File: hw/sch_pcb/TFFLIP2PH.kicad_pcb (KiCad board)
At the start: 2 copper layers, 65.3 x 15.7 mm, 2 parts, among them J1 Flipper_Zero

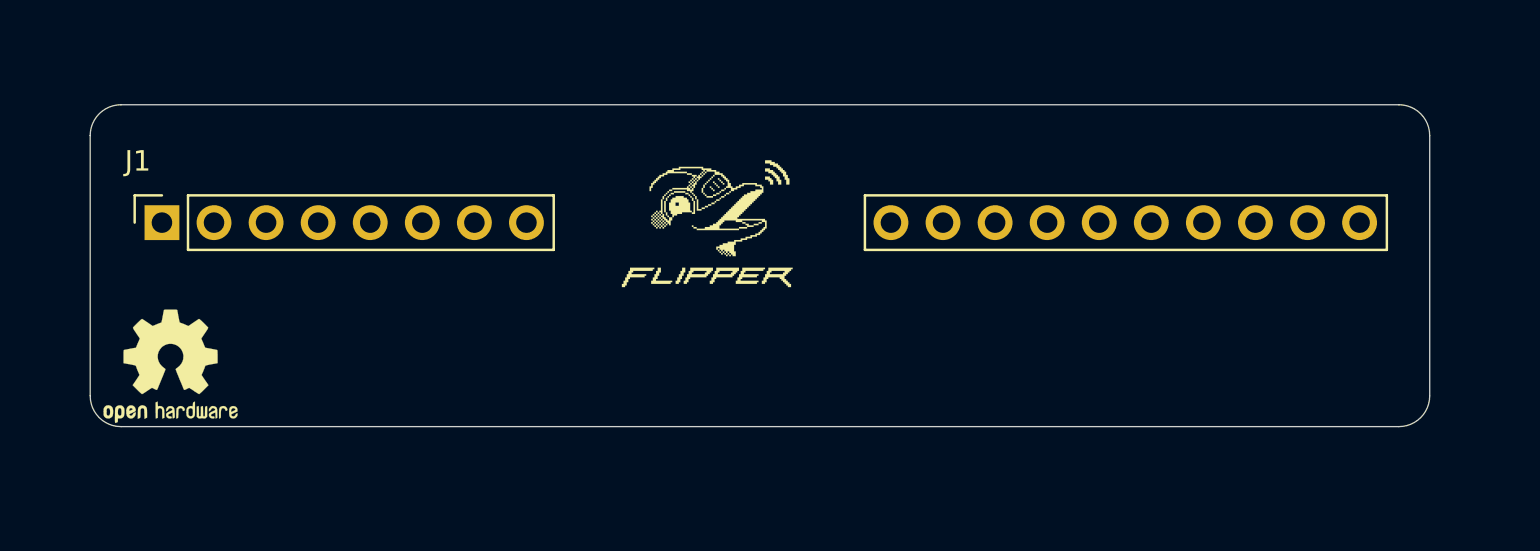
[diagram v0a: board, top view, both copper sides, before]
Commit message: Swap board sides to match top view on flipper zero.
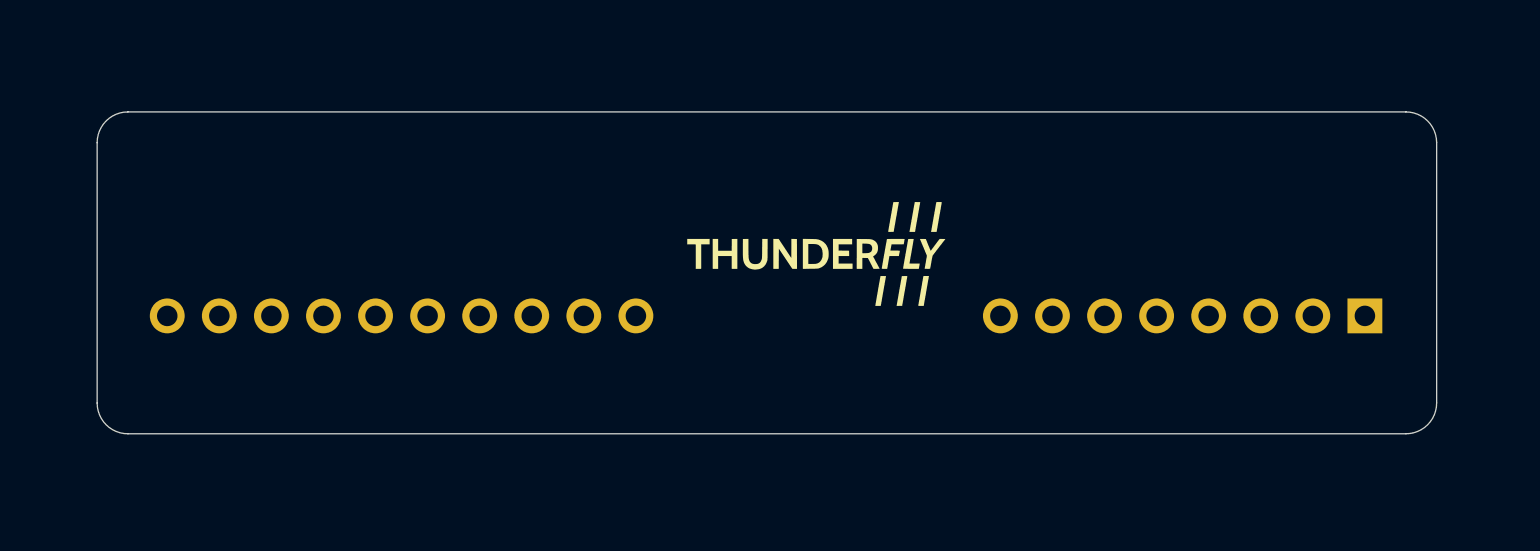
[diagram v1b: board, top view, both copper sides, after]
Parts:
- removed REF**: OSHW-Logo2_7.3x6mm_SilkScreen, Symbol:OSHW-Logo2_7.3x6mm_SilkScreen
- added G1: LOGO, TF_LOGA:TF 14x6,6, F.Cu at (144.4, 114.5)
- J1: moved to B.Cu
- moved J1 58.9 mm to (171.3, 117.5), turned to 180 degrees

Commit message: Fix pin-header orientation.
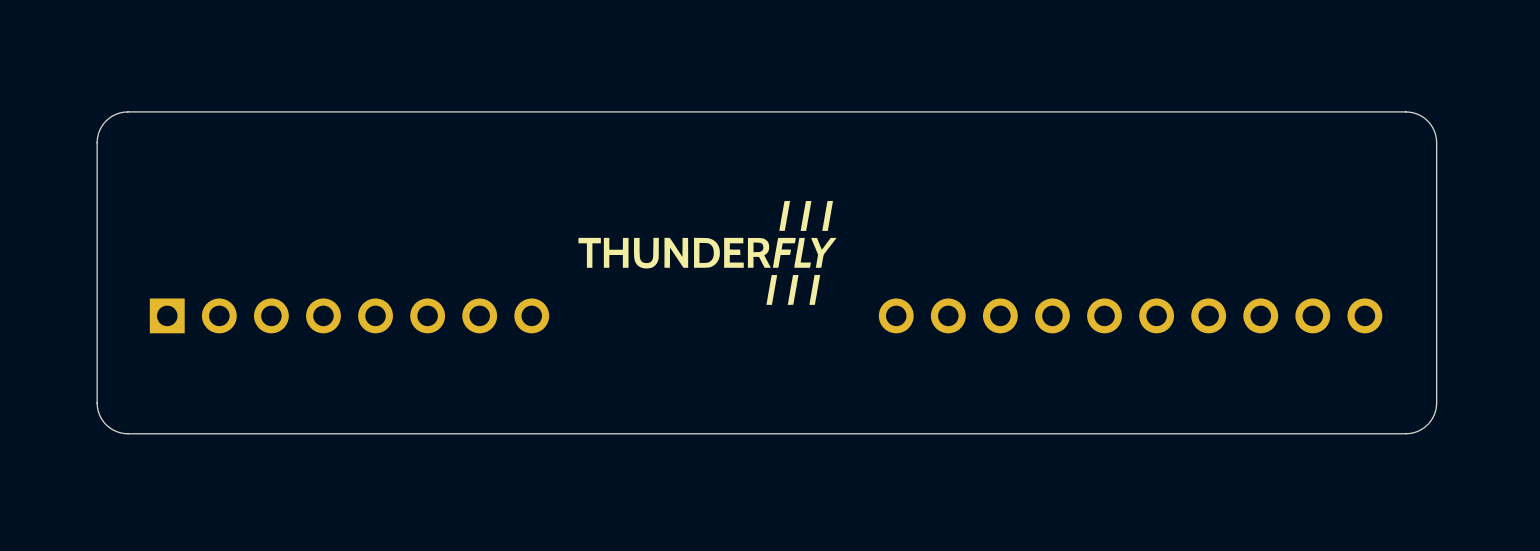
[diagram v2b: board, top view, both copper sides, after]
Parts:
- moved J1 58.4 mm to (112.8, 117.5), turned to 0 degrees
- moved G1 5.31 mm to (139.1, 114.5)

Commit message: Restore accidentally deleted OSHW logo.
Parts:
- added REF**: OSHW-Logo2_7.3x6mm_SilkScreen, Symbol:OSHW-Logo2_7.3x6mm_SilkScreen, B.Cu at (170.4, 111.5)

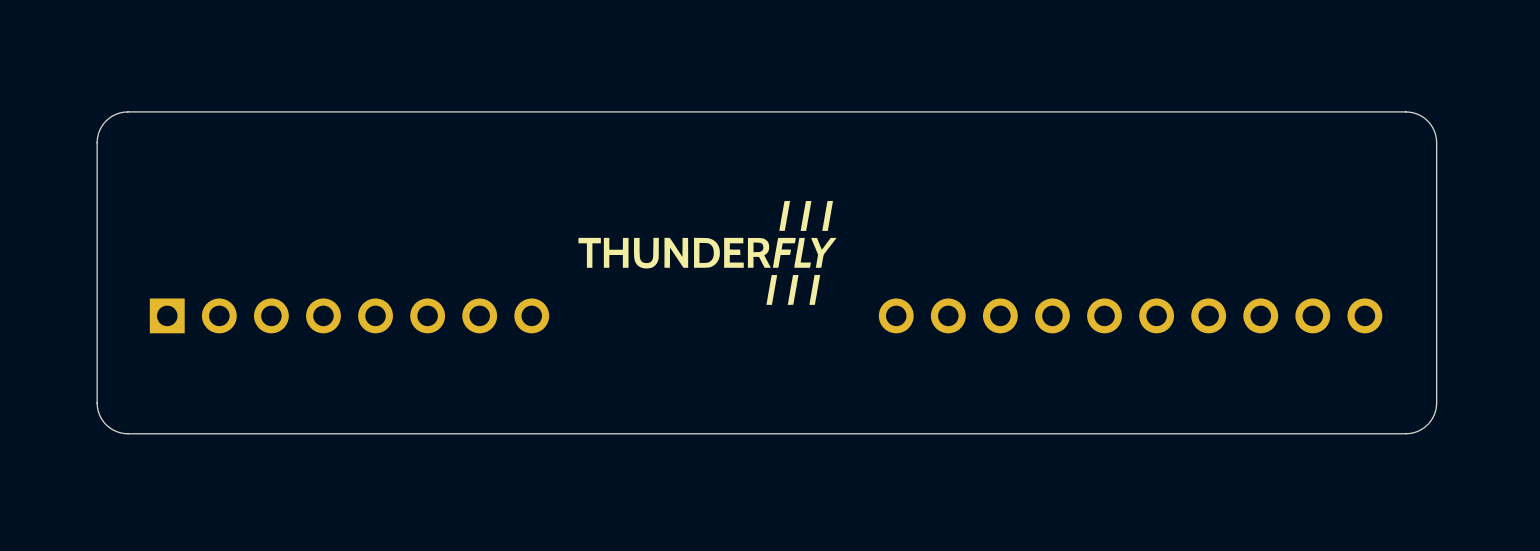
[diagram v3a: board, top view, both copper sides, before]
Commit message: Initial set of connectors.
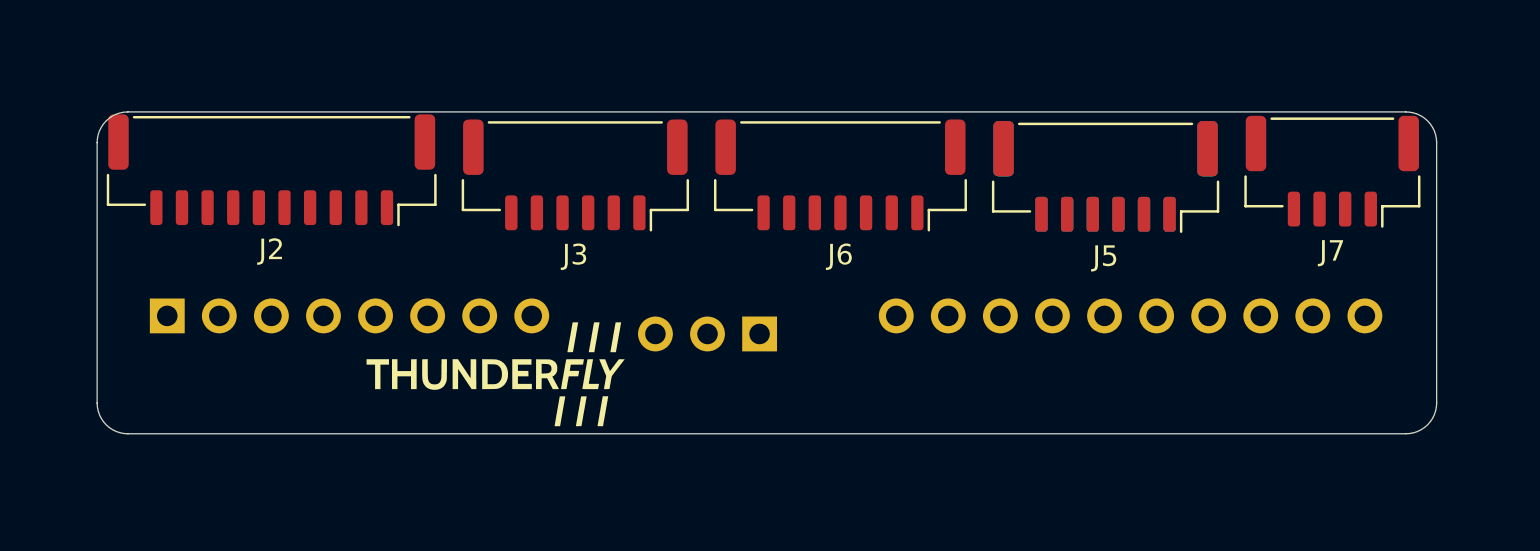
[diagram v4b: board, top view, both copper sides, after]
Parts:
- added J2: SM10B-GHS-TB, Connector_JST:JST_GH_SM10B-GHS-TB_1x10-1MP_P1.25mm_Horizontal, F.Cu at (117.9, 110.4)
- added J3: SM06B-GHS-TB, Connector_JST:JST_GH_SM06B-GHS-TB_1x06-1MP_P1.25mm_Horizontal, F.Cu at (132.7, 110.7)
- added J4: Angled Pinheader, Connector_PinHeader_2.54mm:PinHeader_1x03_P2.54mm_Horizontal, B.Cu at (141.7, 118.4)
- added J5: SM06B-GHS-TB, Connector_JST:JST_GH_SM06B-GHS-TB_1x06-1MP_P1.25mm_Horizontal, F.Cu at (158.6, 110.7)
- added J6: SM07B-GHS-TB, Connector_JST:JST_GH_SM07B-GHS-TB_1x07-1MP_P1.25mm_Horizontal, F.Cu at (145.7, 110.7)
- added J7: SM04B-GHS-TB, Connector_JST:JST_GH_SM04B-GHS-TB_1x04-1MP_P1.25mm_Horizontal, F.Cu at (169.7, 110.5)
- added J8: SM06B-GHS-TB, Connector_JST:JST_GH_SM06B-GHS-TB_1x06-1MP_P1.25mm_Horizontal, B.Cu at (158.6, 110.7)
- moved G1 11.9 mm to (128.8, 120.4)

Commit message: Routing in progress.
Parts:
- added J9: SM08B-GHS-TB, Connector_JST:JST_GH_SM08B-GHS-TB_1x08-1MP_P1.25mm_Horizontal, B.Cu at (155.0, 110.5)
- moved J8 31.6 mm to (127.0, 110.5)
- moved J2 0.37 mm to (118.3, 110.5)
- moved J3 0.33 mm to (133.0, 110.5)
- moved J5 0.27 mm to (158.7, 110.5)
- moved J6 0.26 mm to (145.9, 110.5)
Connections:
- J1 pad 10: unconnected-(J1-PA14-Pad10) -> /TIMEPULSE
- J1 pad 12: unconnected-(J1-PA13-Pad12) -> /EXTINT
- J1 pad 13: unconnected-(J1-PB6-Pad13) -> /TXD
- J1 pad 14: unconnected-(J1-PB7-Pad14) -> /RXD
- J1 pad 15: unconnected-(J1-PC1-Pad15) -> /SDA
- J1 pad 16: unconnected-(J1-PC0-Pad16) -> /SCL
- J1 pad 17: unconnected-(J1-PB14-Pad17) -> /BUZZER
- J1 pad 2: unconnected-(J1-PA7-Pad2) -> /MOSI
- J1 pad 3: unconnected-(J1-PA6-Pad3) -> /#CTS
- J1 pad 4: unconnected-(J1-PA4-Pad4) -> /SS1
- J1 pad 5: unconnected-(J1-PB3-Pad5) -> /#RTS
- J1 pad 6: unconnected-(J1-PB2-Pad6) -> /SS2
- J1 pad 7: unconnected-(J1-PC3-Pad7) -> /GEO_STAT
- J2 pad 1: +5VA -> +5V
- J2 pad 2: /RX -> /TXD
- J2 pad 3: /TX -> /RXD
- J2 pad 4: /SCL1 -> /SCL
- J2 pad 5: /SDA1 -> /SDA
- J2 pad 6: /SAFETY_SW -> /GEO_STAT
- J2 pad 7: /SAFETY_SW_LED -> /EXTINT
- J2 pad 8: /SAFE_VCC -> +3.3V
- J3 pad 2: /RX -> /TXD
- J3 pad 3: /TX -> /RXD
- J3 pad 4: /I2C2.SCL -> /SCL
- J3 pad 5: /I2C2.SDA -> /SDA
- J4 pad 1: /PWM -> /MOSI
- J6 pad 2: /SCK -> /#RTS
- J6 pad 3: /MISO -> /#CTS
- J6 pad 5: /#CS -> /SS1
- J6 pad 6: unconnected-(J6-Pad6) -> /SS2
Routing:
- net +5V: track 0.00 -> 107.3 mm
- net /SCL: track 0.00 -> 80.9 mm, vias 0 -> 2
- net /SDA: track 0.00 -> 73.7 mm, vias 0 -> 2
- net /RXD: track 0.00 -> 66.0 mm, vias 0 -> 7
- net /BUZZER: track 0.00 -> 64.1 mm
- net /#CTS: track 0.00 -> 54.5 mm, vias 0 -> 1
- net /#RTS: track 0.00 -> 51.2 mm, vias 0 -> 2
- net +3.3V: track 0.00 -> 49.9 mm, vias 0 -> 1
- net /GEO_STAT: track 0.00 -> 48.0 mm, vias 0 -> 2
- net /EXTINT: track 0.00 -> 46.5 mm, vias 0 -> 1
- net /MOSI: track 0.00 -> 37.1 mm
- net /SS1: track 0.00 -> 30.4 mm
- net /SS2: track 0.00 -> 22.1 mm
- net /TXD: track 0.00 -> 16.1 mm, vias 0 -> 2
- net GND: track 0.00 -> 14.4 mm, vias 0 -> 6
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- added copper zone on B.Cu, net GND
- added copper zone on F.Cu, net GND
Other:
- rule pad_to_mask_clearance: 0 -> 0.05

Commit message: Fully routed PCB.
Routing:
- net +5V: track 107.3 -> 165.7 mm
- net GND: track 14.4 -> 63.8 mm, vias 6 -> 10
- net /TXD: track 16.1 -> 53.4 mm, vias 2 -> 3
- net /RXD: track 66.0 -> 62.4 mm
- net /GEO_STAT: track 48.0 -> 45.3 mm
- net /#RTS: track 51.2 -> 49.0 mm
- net /MOSI: track 37.1 -> 38.1 mm
- net /SDA: track 73.7 -> 72.7 mm
- net /BUZZER: track 64.1 -> 63.3 mm
- net /EXTINT: track 46.5 -> 47.1 mm

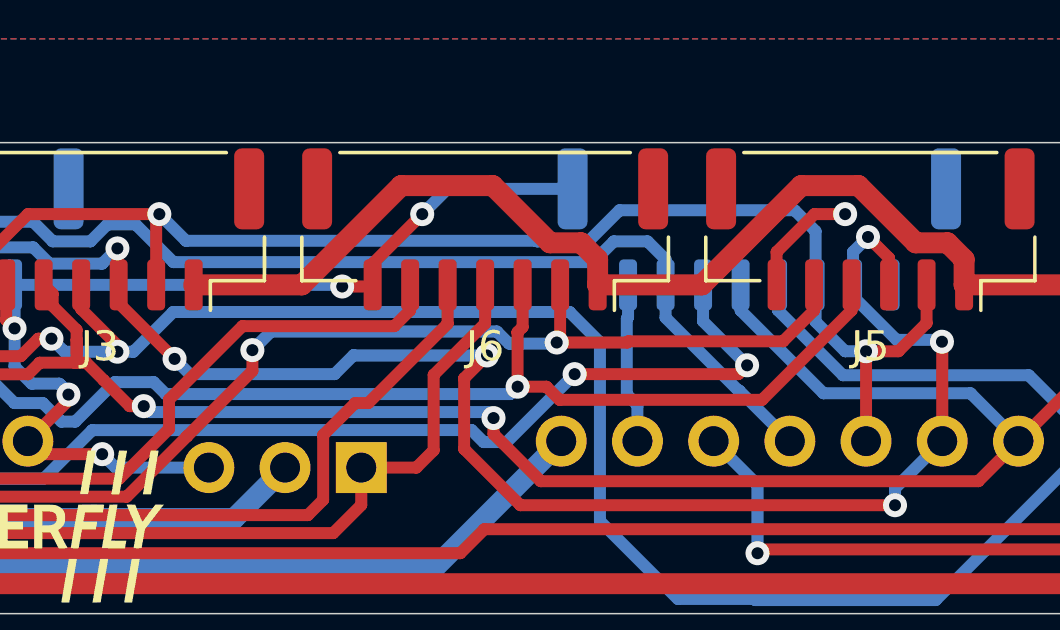
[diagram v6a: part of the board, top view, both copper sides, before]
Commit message: Fix DRC errors.
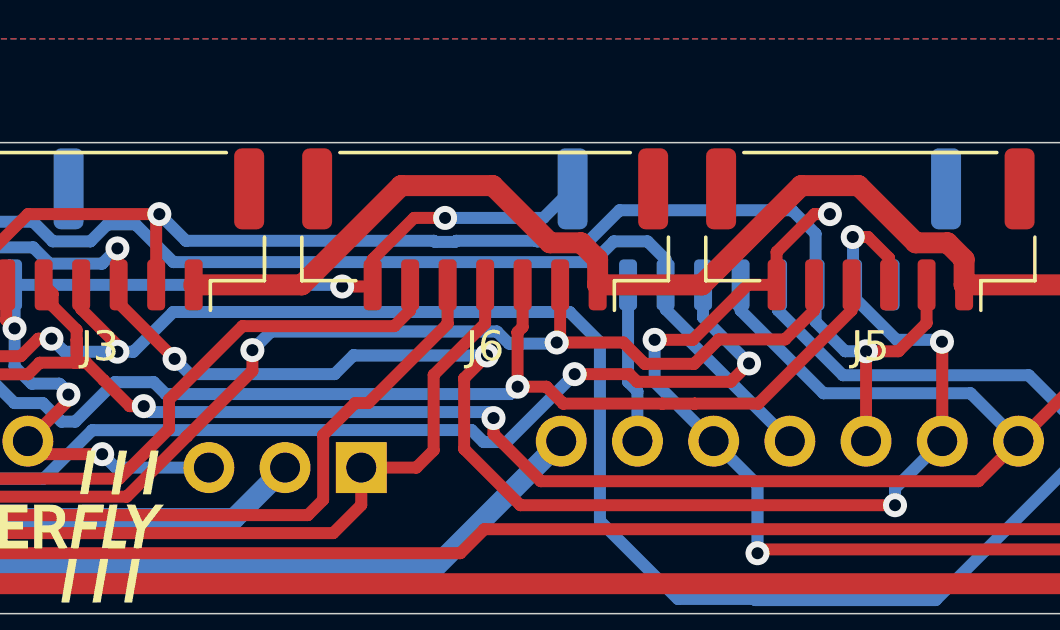
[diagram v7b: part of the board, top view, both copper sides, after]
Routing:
- net GND: track 63.8 -> 72.4 mm, vias 10 -> 11
- net /#RTS: track 49.0 -> 49.6 mm

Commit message: Improve layout and silkscreen.
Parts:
- G1: footprint TF_LOGA:TF 14x6,6 -> TF_LOGA:TF 10x4,7
- moved G1 40.7 mm to (169.5, 120.6)
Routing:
- net GND: track 72.4 -> 79.5 mm, vias 11 -> 12
- net /#RTS: track 49.6 -> 49.0 mm
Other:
- board text added: "+5V"
- board text added: "GND"
- board text added: "GPS"
- board text added: "GPS&SAFETY"
- board text added: "I2C"
- board text added: "SPI"
- board text added: "TF Payload"
- board text added: "Telemetry to Peripheral"
- board text added: "UART to FMU"
